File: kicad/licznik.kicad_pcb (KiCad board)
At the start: 2 copper layers, 54 x 45.1 mm, 32 parts, among them J1 Display, J2 Micro_SD_Card_Det, J3 Serial CS1, J4 Serial CS2, SW1 Wheel, SW2 Crank, SW3 Backlight, SW4 Right, SW5 Select, SW6 Left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

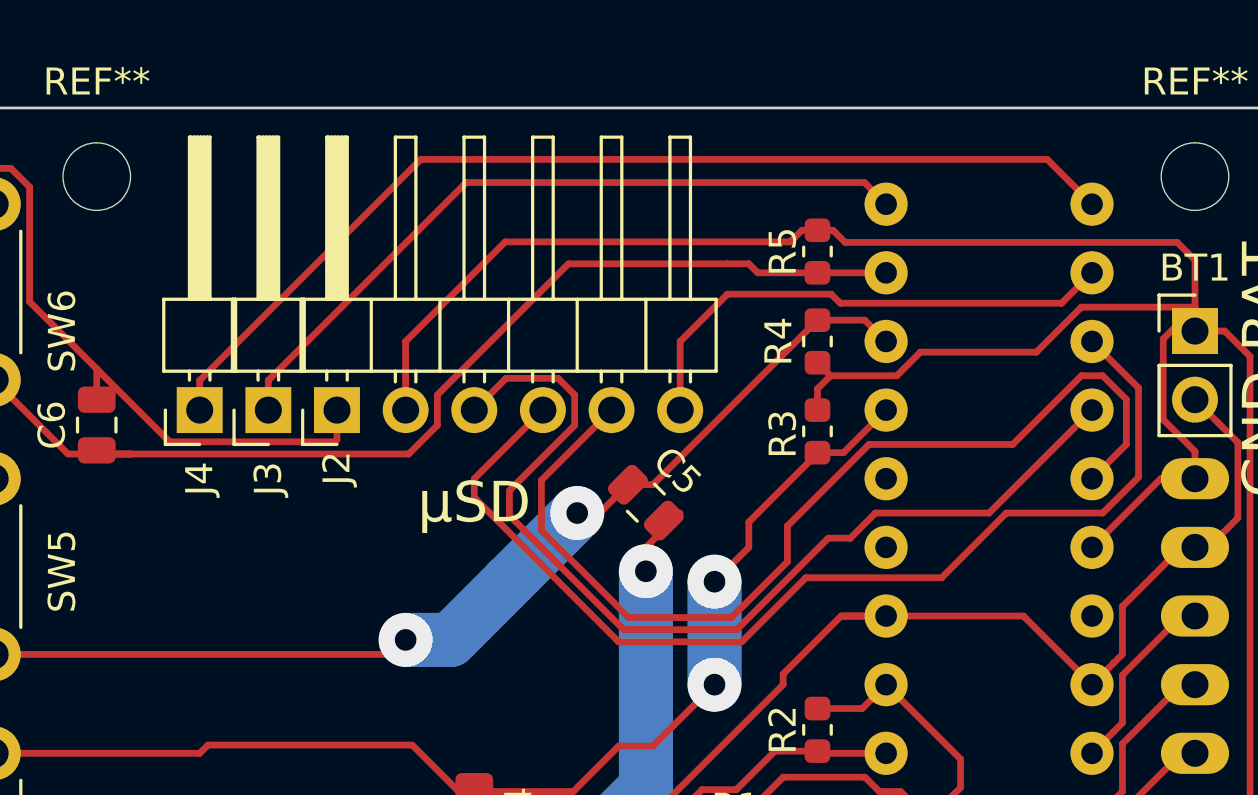
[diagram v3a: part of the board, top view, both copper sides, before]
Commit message: PCB: Stick out the IO header
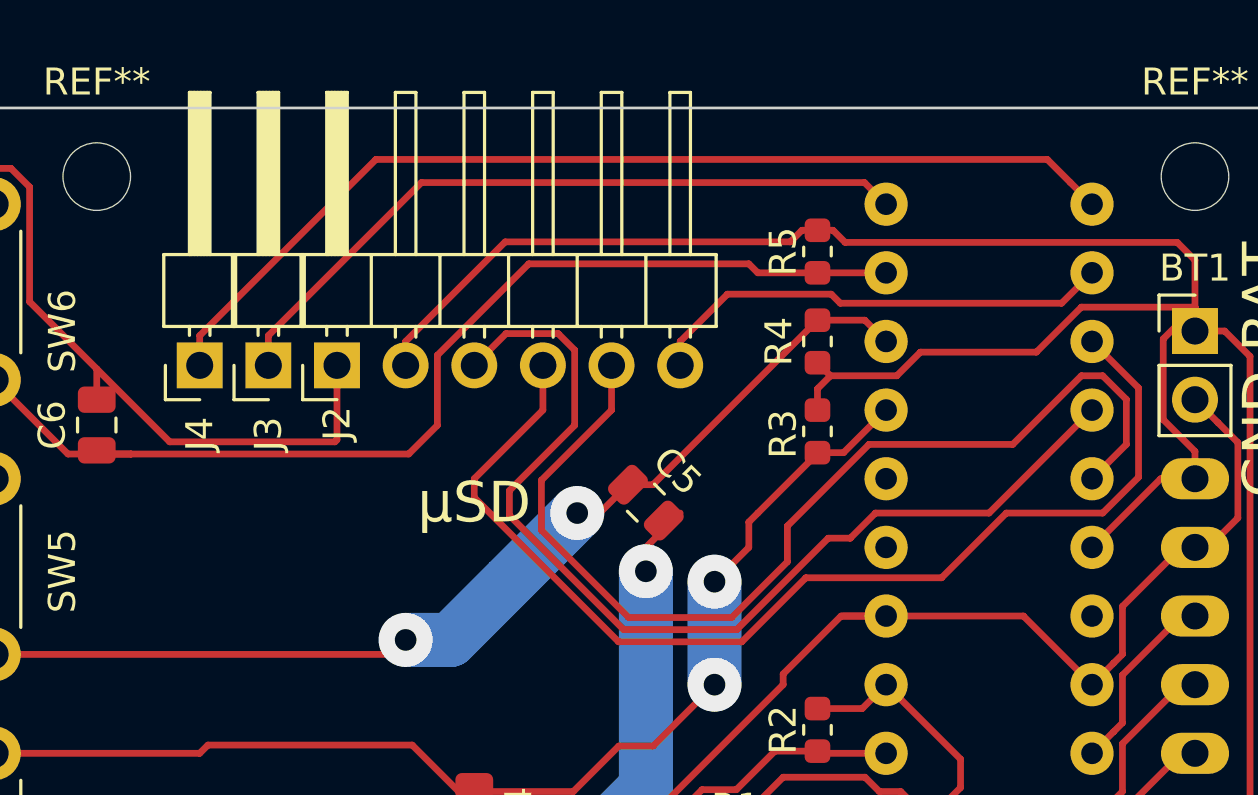
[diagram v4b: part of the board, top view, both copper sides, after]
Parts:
- moved J2 1.66 mm to (55.9, 165.1)
- moved J3 1.66 mm to (53.3, 165.1)
- moved J4 1.66 mm to (50.8, 165.1)
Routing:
- net +BATT: track 144.5 -> 142.9 mm
- net Net-(J2-Pad5): track 36.8 -> 38.5 mm
- net Net-(J2-Pad3): track 39.3 -> 41.0 mm
- net Net-(J2-Pad2): track 19.1 -> 17.5 mm
- net GND: track 194.7 -> 196.4 mm
- net Net-(J2-Pad7): track 36.6 -> 38.2 mm
- net Net-(C6-Pad1): track 45.7 -> 46.6 mm
- net Net-(J4-Pad1): track 38.2 -> 37.5 mm
- net Net-(J3-Pad1): track 27.3 -> 26.6 mm

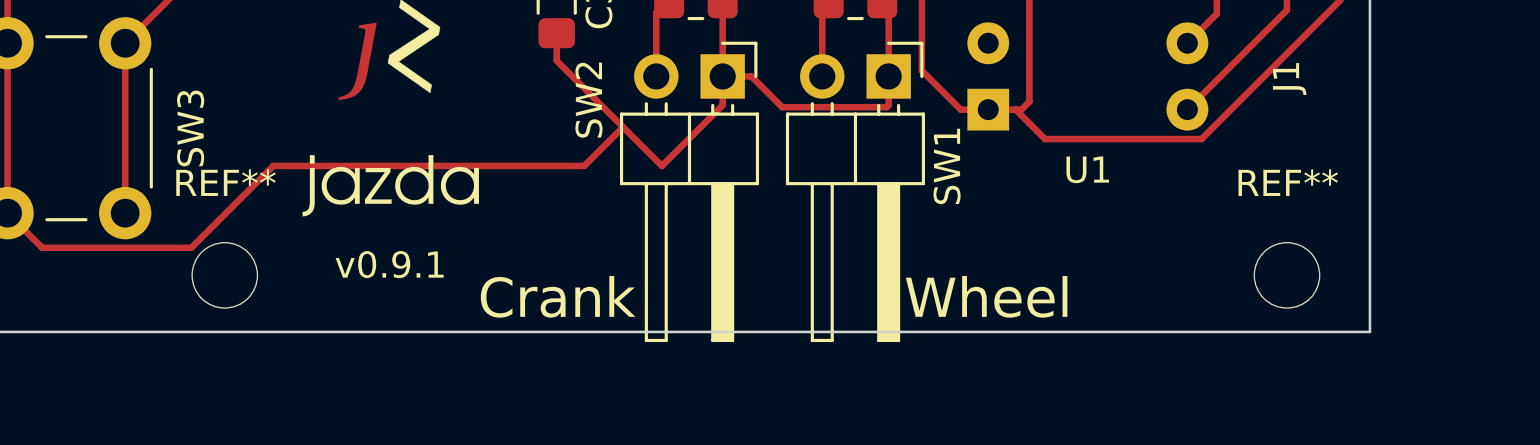
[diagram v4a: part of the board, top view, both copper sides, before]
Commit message: PCB: Move holes description away from polluting the board
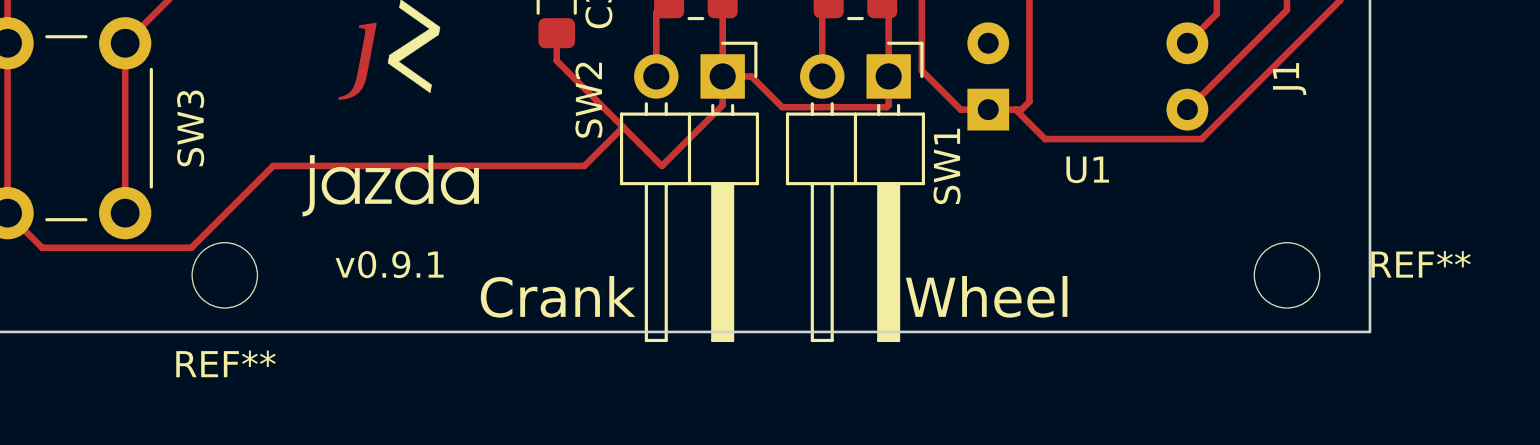
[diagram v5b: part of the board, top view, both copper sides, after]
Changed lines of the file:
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@@
     (tags "mounting hole 2.5mm no annular")
     (attr virtual)
-    (fp_text reference REF** (at 0 -3.5) (layer F.SilkS)
+    (fp_text reference REF** (at 5.08 -0.375) (layer F.SilkS)
       (effects (font (size 1 1) (thickness 0.15)))
     )
@@
     (tags "mounting hole 2.5mm no annular")
     (attr virtual)
-    (fp_text reference REF** (at 0 -3.5) (layer F.SilkS)
+    (fp_text reference REF** (at 0 3.435) (layer F.SilkS)
       (effects (font (size 1 1) (thickness 0.15)))
     )

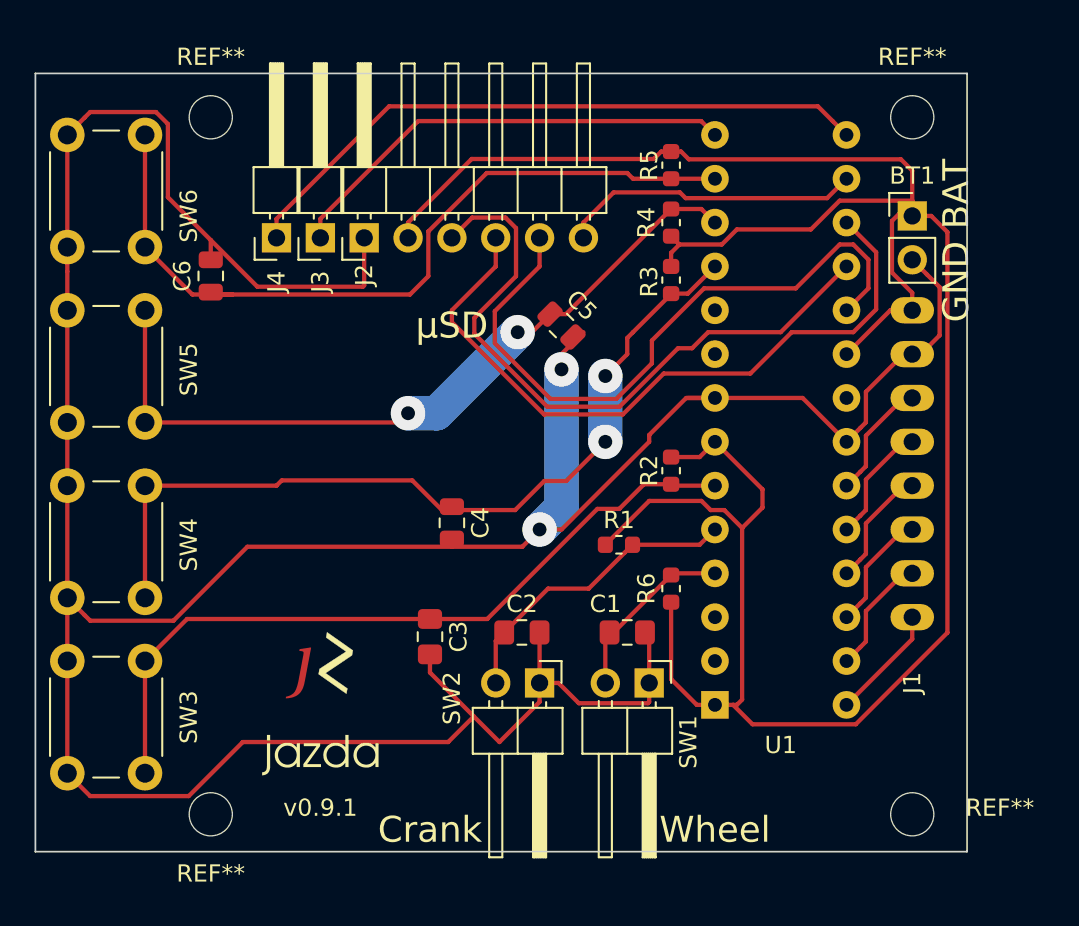
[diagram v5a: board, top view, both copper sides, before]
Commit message: PCB: Use optional RTC capacitor
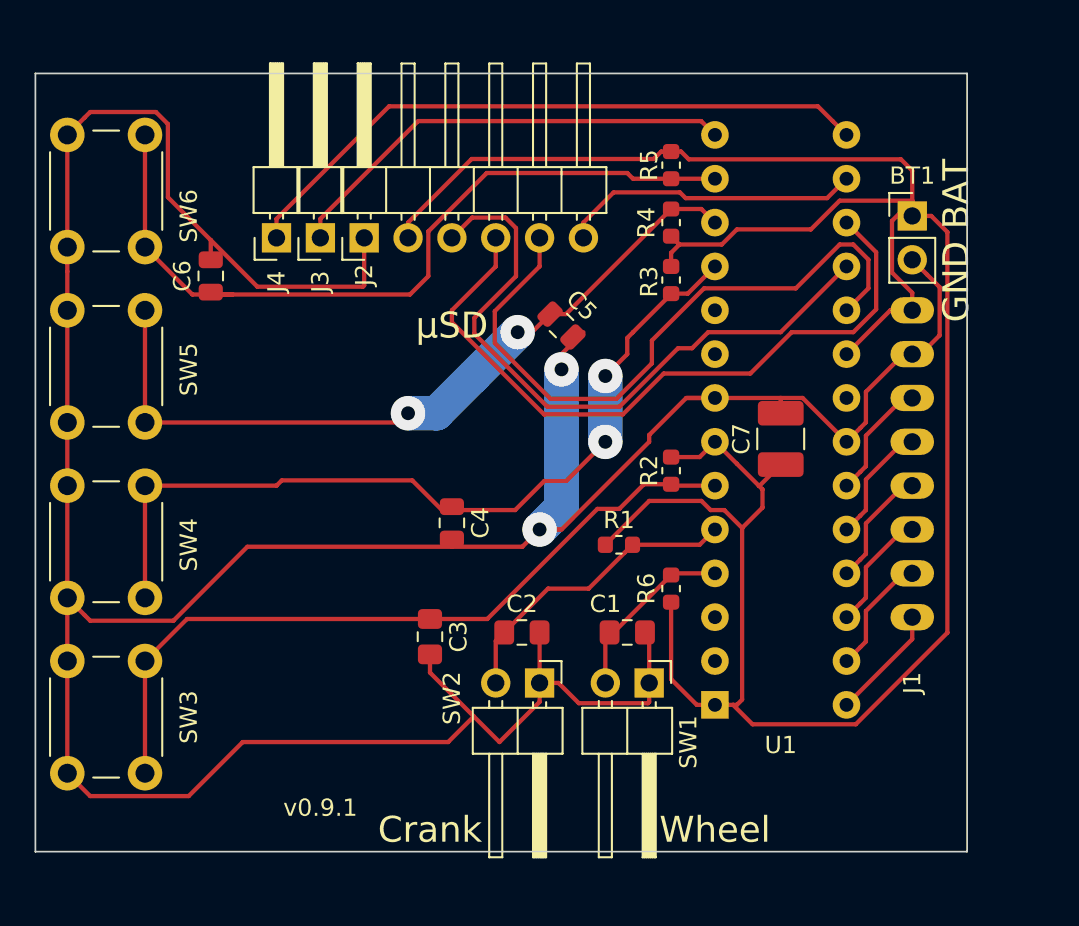
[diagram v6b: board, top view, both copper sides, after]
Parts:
- removed REF** (x4): MountingHole_2.5mm, MountingHole:MountingHole_2.5mm
- removed REF**: OSHW-Logo2_7.3x6mm_SilkScreen, Symbol:OSHW-Logo2_7.3x6mm_SilkScreen
- removed REF**: KiCad-Logo2_6mm_SilkScreen, Symbol:KiCad-Logo2_6mm_SilkScreen
- removed logo: G***, Licznik:logo_half
- removed logo: G***, Licznik:logo_ss
- added C7: 100µF, Capacitor_SMD:C_1210_3225Metric_Pad1.42x2.65mm_HandSolder, F.Cu at (80.0, 176.7)
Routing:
- net +BATT: track 142.9 -> 144.7 mm
- net GND: track 196.4 -> 197.3 mm
